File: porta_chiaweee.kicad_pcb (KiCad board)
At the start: 2 copper layers, 52.2 x 52.2 mm, 3 parts, among them SW1 SW_Push

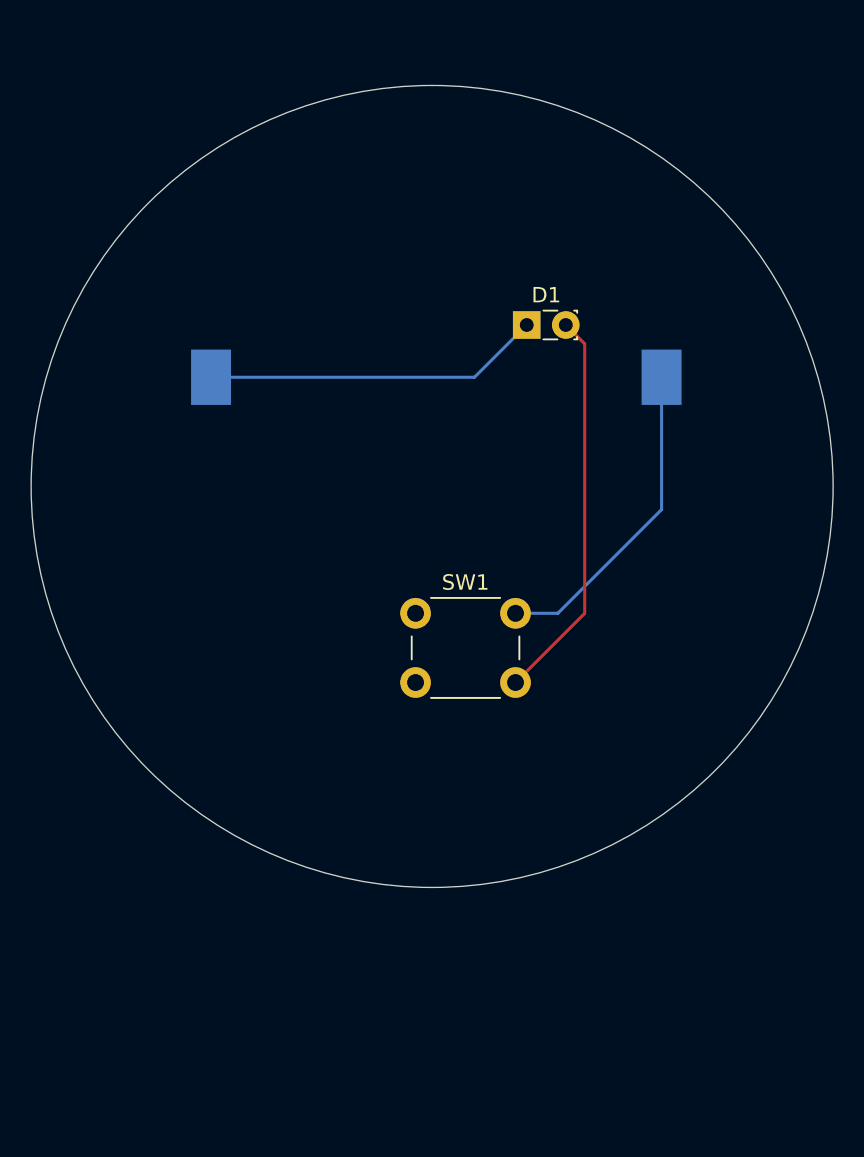
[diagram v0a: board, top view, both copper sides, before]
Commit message: forma pcb e buco
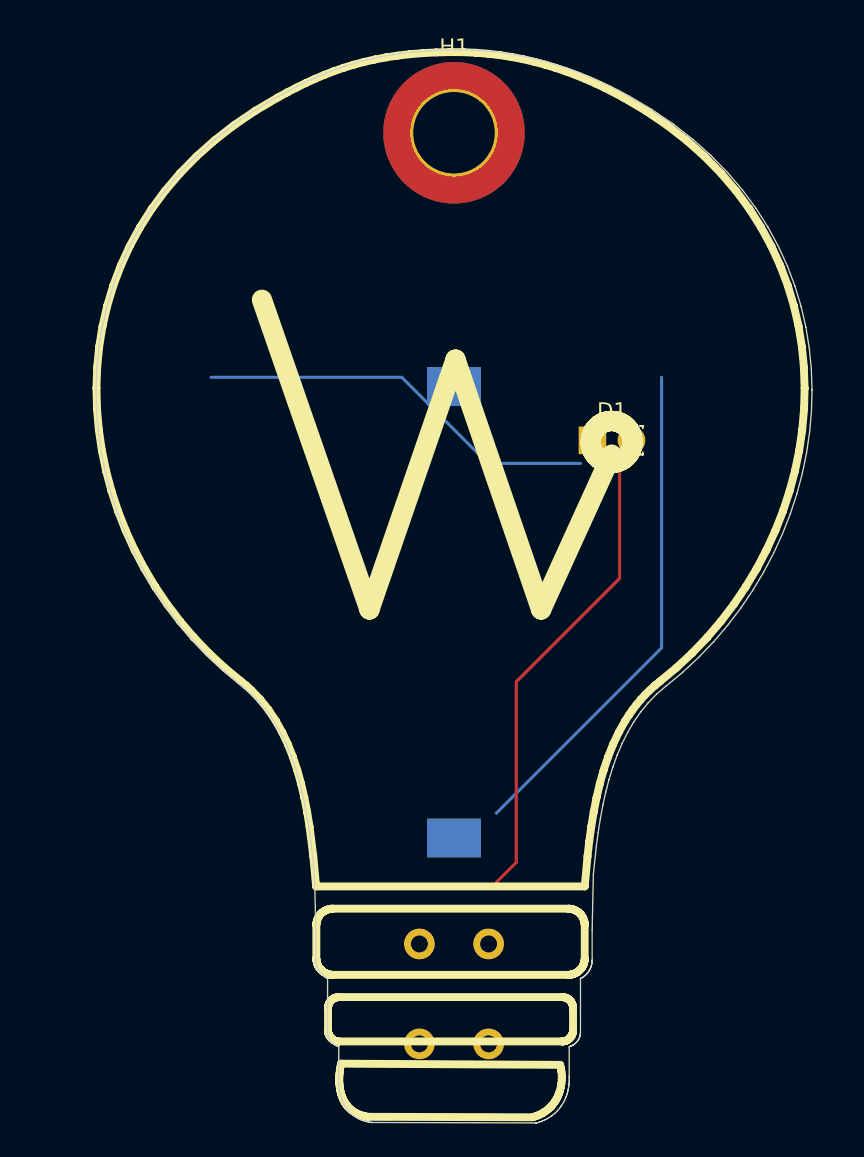
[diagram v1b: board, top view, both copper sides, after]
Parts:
- added H1: MountingHole, MountingHole:MountingHole_5.3mm_M5_DIN965_Pad_TopBottom, F.Cu at (125.0, 59.0)
- BT1: footprint Battery:BatteryHolder_Keystone_1060_1x2032 -> Battery:BatteryHolder_Keystone_1058_1x2032
- SW1: moved to B.Cu
- moved SW1 21.5 mm to (122.8, 111.8), turned to -90 degrees
- moved BT1 15.3 mm to (125.0, 90.2), turned to -90 degrees
- moved D1 8.63 mm to (134.0, 79.0)
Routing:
- net Net-(BT1-+): track 20.9 -> 59.2 mm
- net Net-(BT1--): track 21.9 -> 0.00 mm
- net Net-(D1-A): track 25.6 -> 30.6 mm
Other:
- board size 52.2 x 52.2 mm -> 46.6 x 69.8 mm

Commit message: aggiunte librerie nuove e modelli 3D
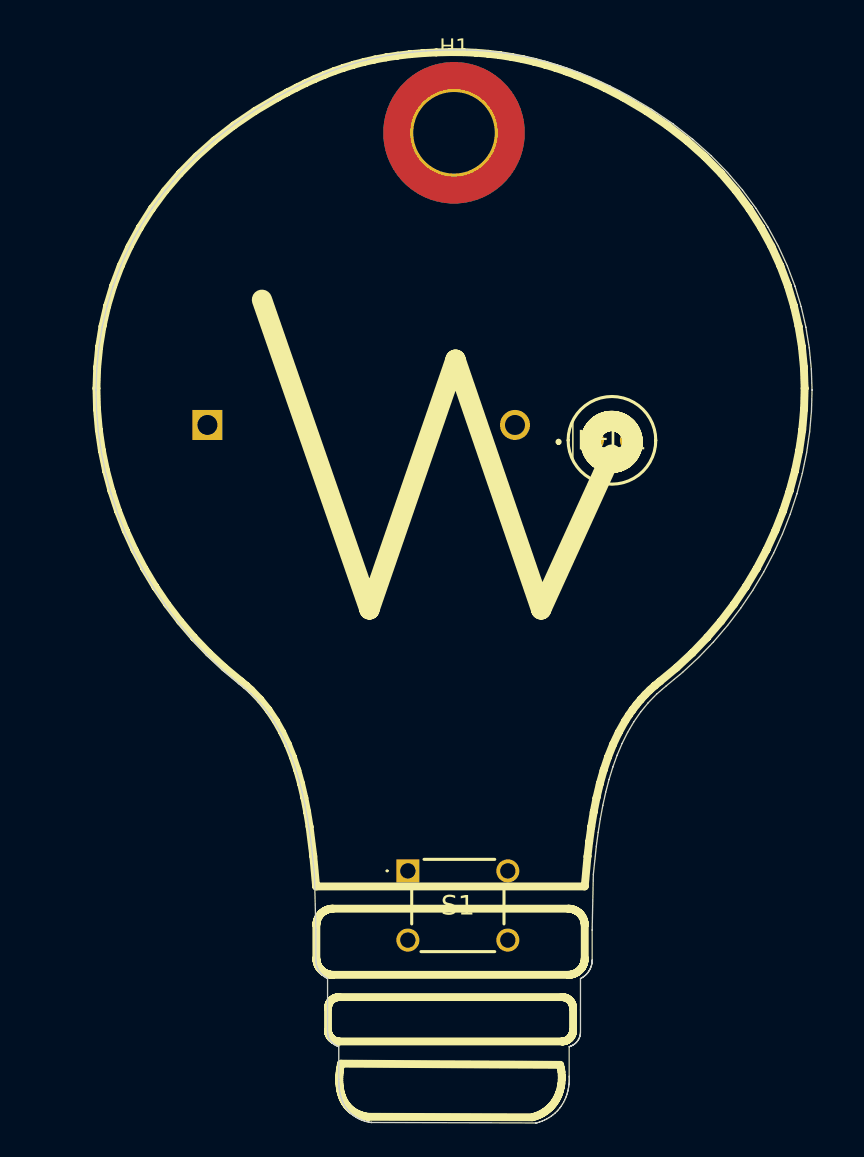
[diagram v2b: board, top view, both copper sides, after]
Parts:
- removed BT1: Battery_Cell, Battery:BatteryHolder_Keystone_1058_1x2032
- removed D1: LED, LED_THT:LED_Rectangular_W3.9mm_H1.8mm
- removed SW1: SW_Push, Button_Switch_THT:SW_PUSH_6mm_H13mm
- added H2: BH-25C-1, components:BH25C1, B.Cu at (109.0, 78.0)
- added LED1: WP7083ZGD_G, components:L53ND, F.Cu at (134.0, 79.0)
- added S1: TS02-66-43-BK-100-LCR-D, components:TS026643BK100LCRD, F.Cu at (122.0, 107.0)
- H1: value MountingHole -> The_hole
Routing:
- net Net-(BT1-+): track 59.2 -> 0.00 mm
- net Net-(D1-A): track 30.6 -> 0.00 mm

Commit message: rooting e nuovo bordo
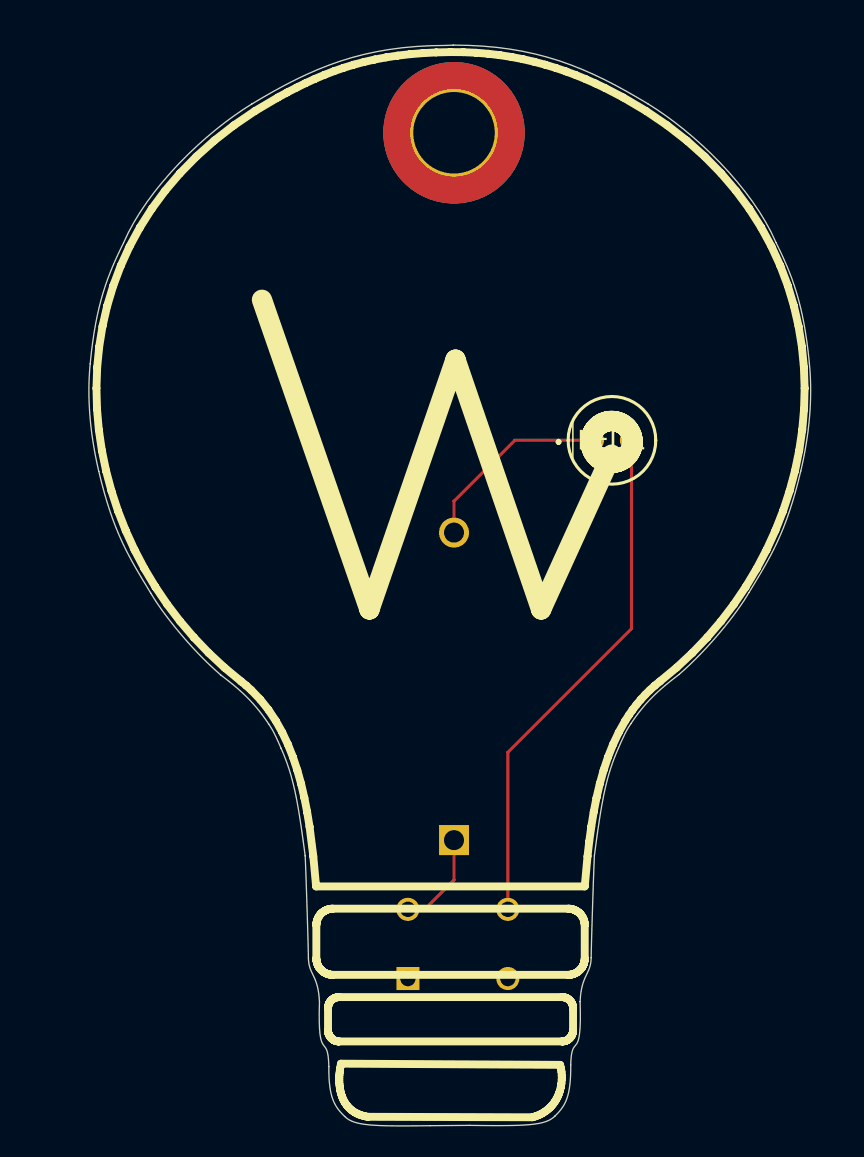
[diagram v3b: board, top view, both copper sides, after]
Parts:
- S1: moved to B.Cu
- moved H2 31.4 mm to (125.0, 105.0), turned to -90 degrees
- moved S1 7.00 mm to (122.0, 114.0)
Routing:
- net Net-(LED1-A): track 0.00 -> 33.8 mm
- net Net-(H2--): track 0.00 -> 12.7 mm
- net Net-(H2-+): track 0.00 -> 6.38 mm
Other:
- board size 46.6 x 69.8 mm -> 46.9 x 70.3 mm

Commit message: aggiunto piano di massa
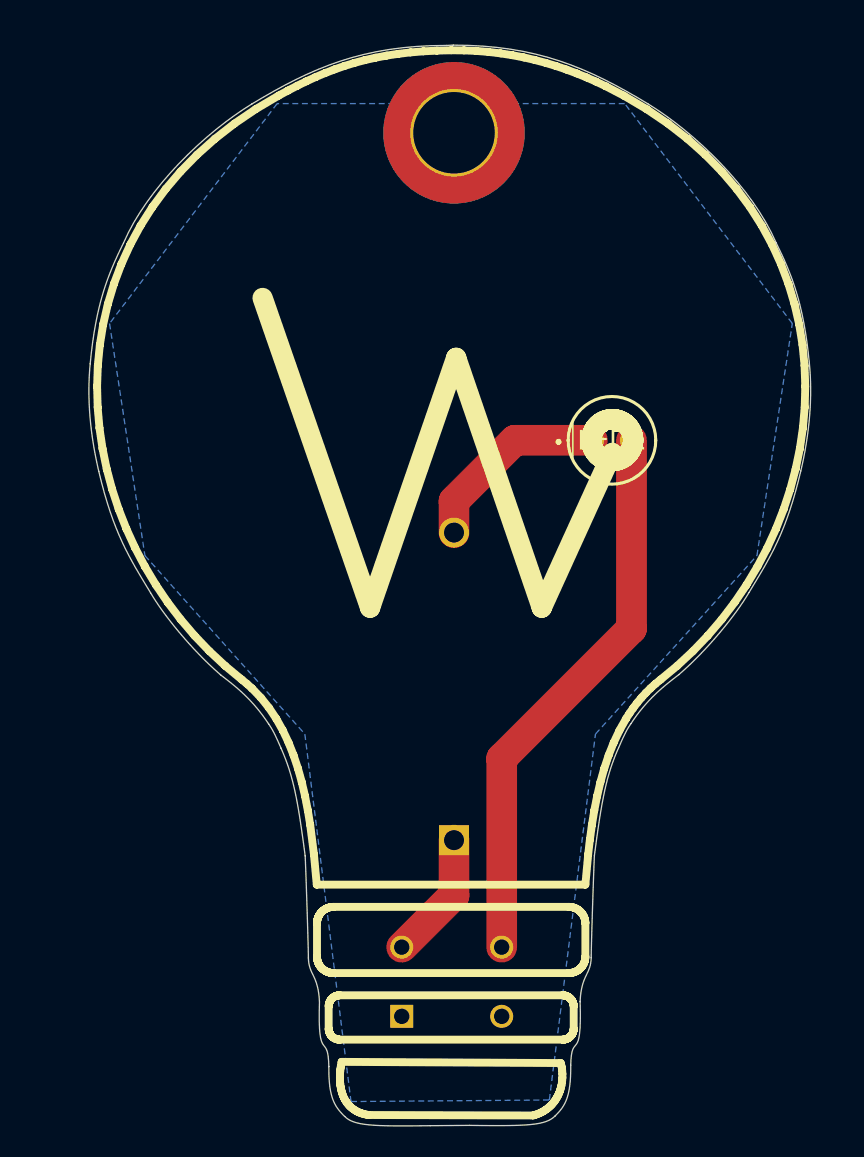
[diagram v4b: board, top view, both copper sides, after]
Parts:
- moved S1 2.49 mm to (121.6, 116.5)
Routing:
- net Net-(LED1-A): track 33.8 -> 36.5 mm
- net Net-(H2-+): track 6.38 -> 8.39 mm
- added copper zone on B.Cu, net (none)
